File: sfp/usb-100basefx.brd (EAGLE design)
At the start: 54 x 29 mm, 52 parts, among them IC1 LD33, IC2 93LC66SN, U1 AX88772BSP, U2 SFP, Y1 25MHz

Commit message: sfp: fixes
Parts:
- BOX1: value HAMMOND-BOX-H -> HAMMOND-BOX-H-1H; device hammond:1551H -> hammond:1551H-1HOLE
- moved R1 1.42 mm to (15.6, 8.94)
- moved R3 0.41 mm to (15.6, 7.52)
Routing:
- net VCCR: track 4.86 -> 5.95 mm
- net USB_VIN: track 110.1 -> 109.2 mm
- net VCC: track 84.0 -> 83.2 mm
- net GND: track 86.1 -> 86.2 mm, vias 27 -> 24
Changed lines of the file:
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@@
 <layer number="27" name="tValues" color="7" fill="1" visible="no" active="yes"/>
 <layer number="28" name="bValues" color="7" fill="1" visible="no" active="yes"/>
-<layer number="29" name="tStop" color="7" fill="3" visible="yes" active="yes"/>
+<layer number="29" name="tStop" color="7" fill="3" visible="no" active="yes"/>
 <layer number="30" name="bStop" color="7" fill="6" visible="no" active="yes"/>
 <layer number="31" name="tCream" color="7" fill="4" visible="no" active="yes"/>
@@
 <text x="9.3472" y="19.7104" size="1.27" layer="121">SFP</text>
 <text x="9.3472" y="18.288" size="1.27" layer="121">rev0</text>
+<hole x="37.0078" y="2.7432" drill="1.5"/>
 </plain>
 <attributes>
@@
 <element name="U$1" library="SparkFun-Connectors" package="USB-MINIB" value="USB-MINIB-5PIN" x="4.6736" y="22.5552"/>
 <element name="U1" library="balto" package="LQFP64-0.4MM-SHORTPAD" value="AX88772BSP" x="35.9664" y="22.352"/>
-<element name="BOX1" library="hammond" package="1551H" value="HAMMOND-BOX-H" x="0" y="0" locked="yes"/>
+<element name="BOX1" library="hammond" package="1551H-1HOLE" value="HAMMOND-BOX-H-1H" x="0" y="0" locked="yes"/>
 <element name="C2" library="rcl" package="C0603" value="1u" x="12.5984" y="7.112" rot="MR0"/>
 <element name="C5" library="rcl" package="C0603" value="3p3" x="26.6192" y="22.352" rot="R90"/>
@@
 <element name="C30" library="rcl" package="C0603" value="1u" x="5.4864" y="13.4112" rot="R270"/>
 <element name="C31" library="rcl" package="C0603" value="1u" x="6.7056" y="13.4112" rot="R270"/>
-<element name="R1" library="rcl" package="R0603" value="0" x="15.6464" y="10.3632" rot="MR0"/>
-<element name="R3" library="rcl" package="R0603" value="0" x="15.6464" y="7.112" rot="MR0"/>
+<element name="R1" library="rcl" package="R0603" value="0" x="15.6464" y="8.9408" rot="MR0"/>
+<element name="R3" library="rcl" package="R0603" value="0" x="15.6464" y="7.5184" rot="MR0"/>
 </elements>
 <signals>
@@
 <contactref element="R1" pad="1"/>
 <contactref element="C12" pad="1"/>
-<wire x1="16.4964" y1="10.3632" x2="16.6624" y2="10.3632" width="0.4064" layer="16"/>
-<wire x1="16.6624" y1="10.3632" x2="18.122" y2="8.9036" width="0.4064" layer="16"/>
-<wire x1="18.288" y1="8.9036" x2="18.122" y2="8.9036" width="0.4064" layer="16"/>
-<wire x1="16.4964" y1="7.112" x2="17.8444" y2="7.112" width="0.4064" layer="16"/>
-<wire x1="17.8444" y1="7.112" x2="18.288" y2="7.5556" width="0.4064" layer="16"/>
 <wire x1="18.288" y1="8.9036" x2="18.288" y2="7.5556" width="0.4064" layer="16"/>
 <wire x1="18.288" y1="7.5556" x2="19.2668" y2="7.5556" width="0.4064" layer="16"/>
@@
 <wire x1="41.2496" y1="13.6144" x2="41.2496" y2="10.16" width="0.6096" layer="16"/>
 <wire x1="49.7468" y1="20.9296" x2="49.7468" y2="19.304" width="0.3048" layer="16"/>
+<wire x1="18.288" y1="7.5556" x2="16.5336" y2="7.5556" width="0.4064" layer="16"/>
+<wire x1="16.5336" y1="7.5556" x2="16.4964" y2="7.5184" width="0.4064" layer="16"/>
+<wire x1="18.288" y1="8.9036" x2="16.5336" y2="8.9036" width="0.4064" layer="16"/>
+<wire x1="16.5336" y1="8.9036" x2="16.4964" y2="8.9408" width="0.4064" layer="16"/>
 </signal>
 <signal name="GND">
@@
 <wire x1="28.0416" y1="11.5824" x2="36.576" y2="11.5824" width="0.2032" layer="16"/>
 <wire x1="36.576" y1="11.5824" x2="36.9824" y2="11.9888" width="0.2032" layer="16"/>
-<via x="14.6304" y="8.7376" extent="1-16" drill="0.508"/>
-<via x="16.6624" y="8.7376" extent="1-16" drill="0.508"/>
-<via x="15.6464" y="8.7376" extent="1-16" drill="0.508"/>
 <wire x1="14.224" y1="18.0848" x2="16.0528" y2="16.256" width="0.2032" layer="16"/>
-<wire x1="10.7696" y1="11.176" x2="17.272" y2="11.176" width="0.2032" layer="16"/>
+<wire x1="10.7696" y1="11.176" x2="14.224" y2="11.176" width="0.2032" layer="16"/>
+<wire x1="14.224" y1="11.176" x2="14.4272" y2="10.9728" width="0.2032" layer="16"/>
+<wire x1="14.4272" y1="10.9728" x2="17.0688" y2="10.9728" width="0.2032" layer="16"/>
 <wire x1="10.7696" y1="11.176" x2="10.5664" y2="10.9728" width="0.2032" layer="16"/>
-<wire x1="17.272" y1="11.176" x2="17.8816" y2="11.7856" width="0.2032" layer="16"/>
+<wire x1="17.0688" y1="10.9728" x2="17.8816" y2="11.7856" width="0.2032" layer="16"/>
 <via x="18.0848" y="4.064" extent="1-16" drill="0.508"/>
 <via x="19.1008" y="4.064" extent="1-16" drill="0.508"/>
@@
 <wire x1="42.0624" y1="13.6144" x2="42.0624" y2="14.6304" width="0.2032" layer="16"/>
 <wire x1="42.0624" y1="14.6304" x2="41.2496" y2="15.4432" width="0.2032" layer="16"/>
-<wire x1="36.576" y1="11.5824" x2="36.0968" y2="1.6076" width="0" layer="19" extent="16-16"/>
 </signal>
 <signal name="TD_DP">
@@
 <wire x1="3.048" y1="15.24" x2="3.4544" y2="15.6464" width="0.2032" layer="16"/>
 <wire x1="22.7584" y1="13.4112" x2="17.4752" y2="13.4112" width="0.2032" layer="16"/>
-<wire x1="17.4752" y1="13.4112" x2="16.0528" y2="11.9888" width="0.2032" layer="16"/>
-<wire x1="16.0528" y1="11.9888" x2="5.6896" y2="11.9888" width="0.2032" layer="16"/>
+<wire x1="17.4752" y1="13.4112" x2="15.8496" y2="11.7856" width="0.2032" layer="16"/>
+<wire x1="15.8496" y1="11.7856" x2="14.8336" y2="11.7856" width="0.2032" layer="16"/>
+<wire x1="14.8336" y1="11.7856" x2="14.6304" y2="11.9888" width="0.2032" layer="16"/>
+<wire x1="14.6304" y1="11.9888" x2="5.6896" y2="11.9888" width="0.2032" layer="16"/>
 <wire x1="5.6896" y1="11.9888" x2="3.048" y2="14.6304" width="0.2032" layer="16"/>
 </signal>
@@
 <wire x1="2.6416" y1="15.24" x2="2.2352" y2="15.6464" width="0.2032" layer="16"/>
 <wire x1="22.5552" y1="13.0048" x2="17.6784" y2="13.0048" width="0.2032" layer="16"/>
-<wire x1="17.6784" y1="13.0048" x2="16.256" y2="11.5824" width="0.2032" layer="16"/>
-<wire x1="16.256" y1="11.5824" x2="5.4864" y2="11.5824" width="0.2032" layer="16"/>
+<wire x1="17.6784" y1="13.0048" x2="16.0528" y2="11.3792" width="0.2032" layer="16"/>
+<wire x1="16.0528" y1="11.3792" x2="14.6304" y2="11.3792" width="0.2032" layer="16"/>
+<wire x1="14.6304" y1="11.3792" x2="14.4272" y2="11.5824" width="0.2032" layer="16"/>
+<wire x1="14.4272" y1="11.5824" x2="5.4864" y2="11.5824" width="0.2032" layer="16"/>
 <wire x1="5.4864" y1="11.5824" x2="2.6416" y2="14.4272" width="0.2032" layer="16"/>
 </signal>
@@
 <wire x1="17.4752" y1="3.048" x2="26.8224" y2="3.048" width="0.6096" layer="16"/>
 <wire x1="26.8224" y1="3.048" x2="29.0576" y2="0.8128" width="0.6096" layer="16"/>
-<wire x1="29.0576" y1="0.8128" x2="33.3248" y2="0.8128" width="0.6096" layer="16"/>
-<wire x1="33.3248" y1="0.8128" x2="34.1376" y2="1.6256" width="0.6096" layer="16"/>
-<wire x1="34.1376" y1="1.6256" x2="34.1376" y2="4.064" width="0.6096" layer="16"/>
-<wire x1="34.1376" y1="4.064" x2="35.7632" y2="5.6896" width="0.6096" layer="16"/>
-<wire x1="35.7632" y1="5.6896" x2="38.2016" y2="5.6896" width="0.6096" layer="16"/>
-<wire x1="38.2016" y1="5.6896" x2="40.0304" y2="3.8608" width="0.6096" layer="16"/>
-<wire x1="40.0304" y1="3.8608" x2="40.0304" y2="1.8288" width="0.6096" layer="16"/>
-<wire x1="40.0304" y1="1.8288" x2="41.0464" y2="0.8128" width="0.6096" layer="16"/>
-<wire x1="41.0464" y1="0.8128" x2="43.688" y2="0.8128" width="0.6096" layer="16"/>
+<wire x1="29.0576" y1="0.8128" x2="33.7312" y2="0.8128" width="0.6096" layer="16"/>
+<wire x1="33.7312" y1="0.8128" x2="34.544" y2="1.6256" width="0.6096" layer="16"/>
+<wire x1="34.544" y1="1.6256" x2="34.544" y2="3.8608" width="0.6096" layer="16"/>
+<wire x1="34.544" y1="3.8608" x2="35.3568" y2="4.6736" width="0.6096" layer="16"/>
+<wire x1="35.3568" y1="4.6736" x2="38.2016" y2="4.6736" width="0.6096" layer="16"/>
+<wire x1="38.2016" y1="4.6736" x2="38.8112" y2="4.064" width="0.6096" layer="16"/>
+<wire x1="38.8112" y1="4.064" x2="38.8112" y2="2.032" width="0.6096" layer="16"/>
+<wire x1="38.8112" y1="2.032" x2="40.0304" y2="0.8128" width="0.6096" layer="16"/>
+<wire x1="40.0304" y1="0.8128" x2="43.688" y2="0.8128" width="0.6096" layer="16"/>
 <wire x1="43.688" y1="0.8128" x2="44.5008" y2="1.6256" width="0.6096" layer="16"/>
 <wire x1="44.5008" y1="1.6256" x2="44.5008" y2="2.2352" width="0.6096" layer="16"/>
@@
 <wire x1="13.4112" y1="9.3472" x2="13.4112" y2="10.326" width="0.4064" layer="16"/>
 <wire x1="13.4112" y1="10.326" x2="13.4484" y2="10.3632" width="0.4064" layer="16"/>
-<wire x1="13.4484" y1="10.3632" x2="14.7964" y2="10.3632" width="0.4064" layer="16"/>
+<wire x1="13.4484" y1="10.3632" x2="14.224" y2="10.3632" width="0.4064" layer="16"/>
+<wire x1="14.224" y1="10.3632" x2="14.7964" y2="9.7908" width="0.4064" layer="16"/>
+<wire x1="14.7964" y1="8.9408" x2="14.7964" y2="9.7908" width="0.4064" layer="16"/>
 </signal>
 <signal name="VCCT">
@@
 <wire x1="13.4112" y1="8.128" x2="13.4112" y2="7.1492" width="0.4064" layer="16"/>
 <wire x1="13.4112" y1="7.1492" x2="13.4484" y2="7.112" width="0.4064" layer="16"/>
-<wire x1="13.4484" y1="7.112" x2="14.7964" y2="7.112" width="0.4064" layer="16"/>
+<wire x1="13.4484" y1="7.112" x2="14.39" y2="7.112" width="0.4064" layer="16"/>
+<wire x1="14.39" y1="7.112" x2="14.7964" y2="7.5184" width="0.4064" layer="16"/>
 </signal>
 </signals>

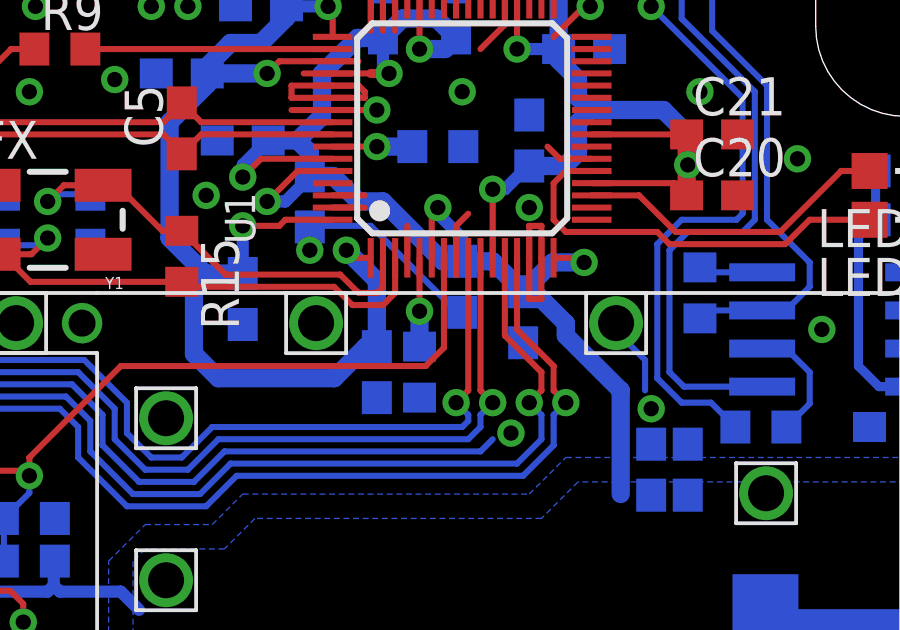
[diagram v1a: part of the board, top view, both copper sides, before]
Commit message: add gnd guard
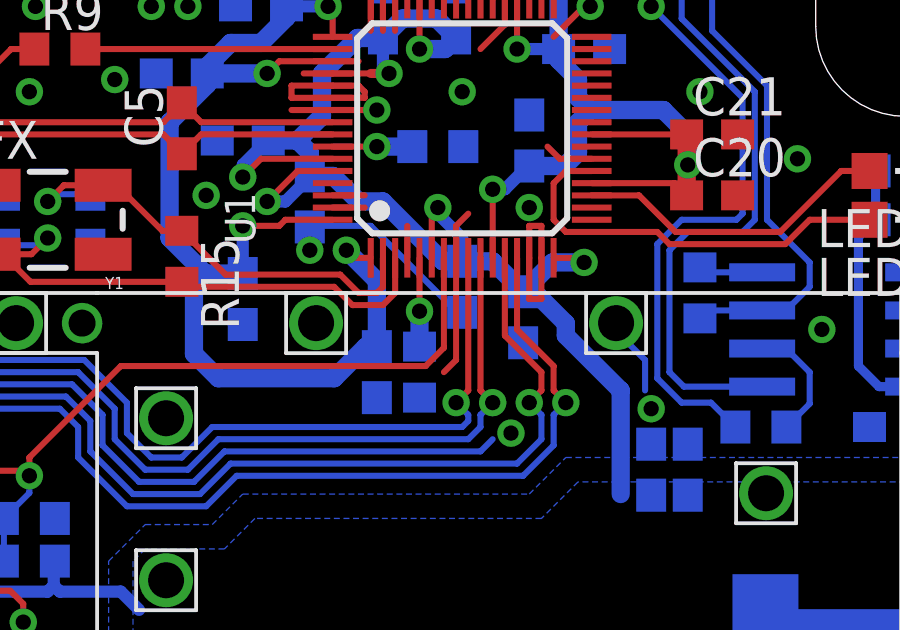
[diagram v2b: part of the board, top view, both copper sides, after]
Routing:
- net GND: track 86.2 -> 90.2 mm
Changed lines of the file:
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@@
 <wire x1="42.0624" y1="13.6144" x2="42.0624" y2="14.6304" width="0.2032" layer="16"/>
 <wire x1="42.0624" y1="14.6304" x2="41.2496" y2="15.4432" width="0.2032" layer="16"/>
+<wire x1="35.7632" y1="18.034" x2="35.7632" y2="14.6304" width="0.2032" layer="1"/>
+<wire x1="35.7632" y1="14.6304" x2="35.3568" y2="14.224" width="0.2032" layer="1"/>
 </signal>
 <signal name="TD_DP">
